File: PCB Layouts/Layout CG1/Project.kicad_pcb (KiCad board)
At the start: 2 copper layers, 15 x 17.5 mm, 11 parts, among them J1 Conn_01x04

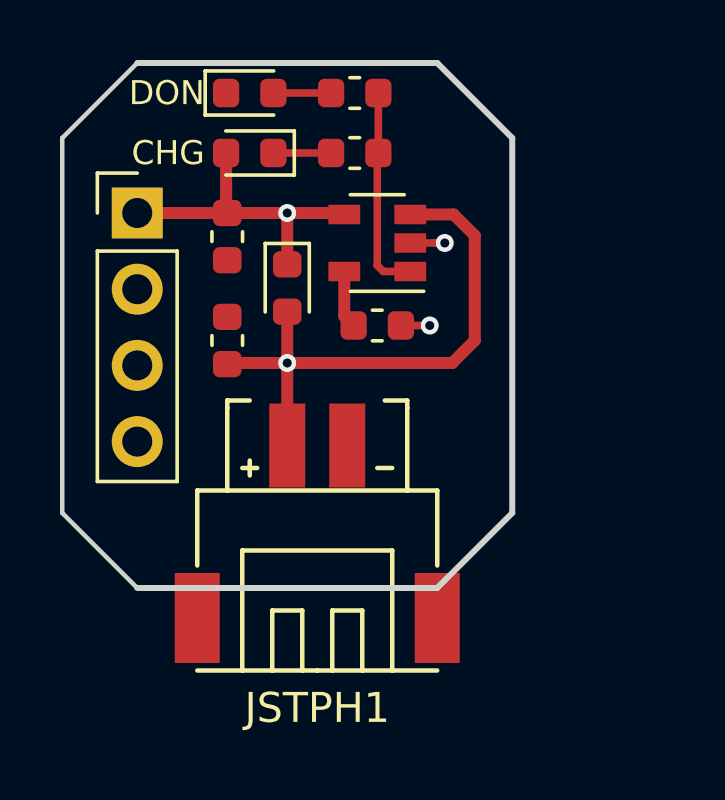
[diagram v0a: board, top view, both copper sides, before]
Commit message: Updated LiPo battery connector footprint and finalized component placement
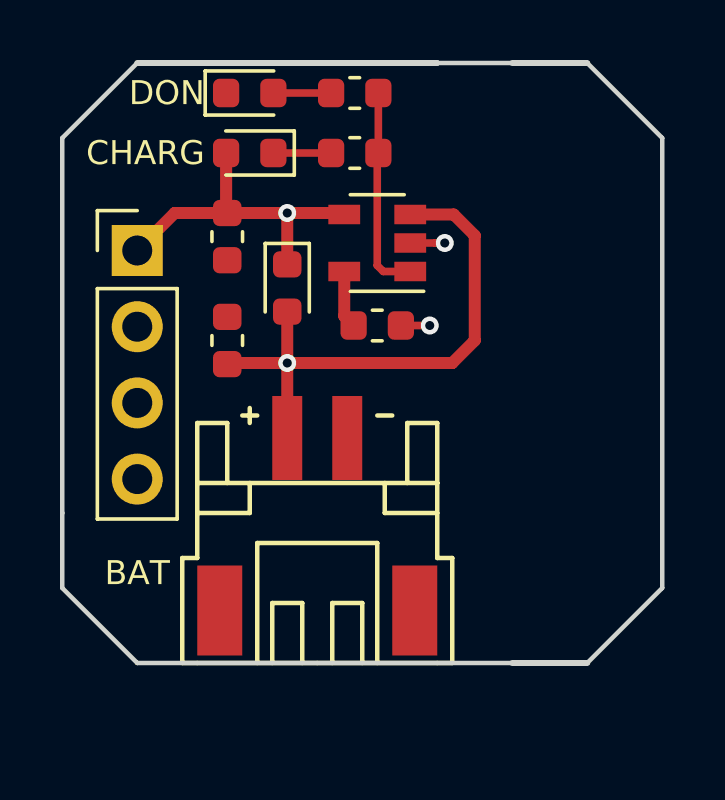
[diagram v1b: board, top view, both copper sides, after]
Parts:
- moved J1 1.25 mm to (100.0, 101.2)
- moved JSTPH1 0.25 mm to (106.0, 112.0)
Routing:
- net VDD: track 10.7 -> 11.2 mm
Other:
- board size 15 x 17.5 mm -> 20 x 20 mm
- board text added: "BAT"
- board text added: "CHARG"
- board text removed: "CHG"

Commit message: Fixed the mounting holes with a simple custom footprint and generated the Gerber files for Layout CG1
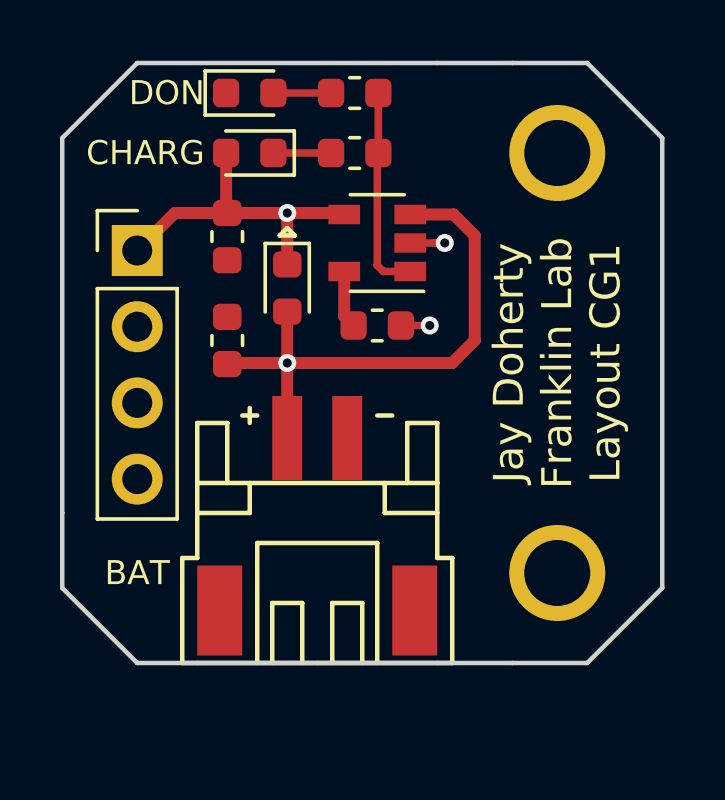
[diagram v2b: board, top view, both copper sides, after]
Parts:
- added MH1: MountingHole, Custom_Footprint_Library:MountingHole_2.2mm, F.Cu at (114.0, 98.0)
- added MH2: MountingHole, Custom_Footprint_Library:MountingHole_2.2mm, F.Cu at (114.0, 112.0)
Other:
- board text added: "Jay Doherty Franklin Lab Layout CG1"
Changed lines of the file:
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@@
   (general
     (thickness 1.6)
-    (drawings 17)
+    (drawings 21)
     (tracks 41)
     (zones 0)
-    (modules 11)
+    (modules 13)
     (nets 10)
   )
@@
   )
   (setup
-    (last_trace_width 0.4)
+    (last_trace_width 0.254)
     (user_trace_width 0.4)
     (trace_clearance 0.254)
@@
     (zone_45_only no)
     (trace_min 0.2)
-    (segment_width 0.2)
+    (segment_width 0.15)
     (edge_width 0.15)
     (via_size 0.6)
@@
     (mod_text_size 1 1)
     (mod_text_width 0.15)
-    (pad_size 1.524 1.524)
-    (pad_drill 0.762)
+    (pad_size 2.2 2.2)
+    (pad_drill 2.2)
     (pad_to_mask_clearance 0.2)
     (aux_axis_origin 0 0)
     (visible_elements FFFFFF7F)
     (pcbplotparams
-      (layerselection 0x010fc_ffffffff)
+      (layerselection 0x010f0_ffffffff)
       (usegerberextensions false)
       (usegerberattributes false)
@@
       (outputformat 1)
       (mirror false)
-      (drillshape 1)
+      (drillshape 0)
       (scaleselection 1)
-      (outputdirectory ""))
+      (outputdirectory "Gerbers/"))
   )
   (net 0 "")
@@
       (effects (font (size 1 1) (thickness 0.15)))
     )
-    (fp_text value 5k (at 2.5 0) (layer F.Fab)
+    (fp_text value 5k (at 0 0) (layer F.Fab)
       (effects (font (size 1 1) (thickness 0.15)))
     )
@@
     )
   )
+  (module Custom_Footprint_Library:MountingHole_2.2mm (layer F.Cu)
+    (at 114 98)
+    (fp_text reference MH1 (at 0 -2.5) (layer F.SilkS) hide
+      (effects (font (size 1 1) (thickness 0.15)))
+    )
+    (fp_text value MountingHole (at 0 2.5) (layer F.Fab) hide
+      (effects (font (size 1 1) (thickness 0.15)))
+    )
+    (pad "" thru_hole circle (at 0 0) (size 3.2 3.2) (drill 2.2) (layers *.Cu *.Mask))
+  )
+  (module Custom_Footprint_Library:MountingHole_2.2mm (layer F.Cu)
+    (at 114 112)
+    (fp_text reference MH2 (at 0 -2.5) (layer F.SilkS) hide
+      (effects (font (size 1 1) (thickness 0.15)))
+    )
+    (fp_text value MountingHole (at 0 2.5) (layer F.Fab) hide
+      (effects (font (size 1 1) (thickness 0.15)))
+    )
+    (pad "" thru_hole circle (at 0 0) (size 3.2 3.2) (drill 2.2) (layers *.Cu *.Mask))
+  )
+  (gr_line (start 105 100.5) (end 104.75 100.75) (layer F.SilkS) (width 0.15))
+  (gr_line (start 105.25 100.75) (end 105 100.5) (layer F.SilkS) (width 0.15))
+  (gr_line (start 104.75 100.75) (end 105.25 100.75) (layer F.SilkS) (width 0.15))
+  (gr_text "Jay Doherty\nFranklin Lab\nLayout CG1" (at 114 105 90) (layer F.SilkS)
+    (effects (font (size 1 1) (thickness 0.15)))
+  )
   (gr_text BAT (at 100 112) (layer F.SilkS)
     (effects (font (size 0.8 0.8) (thickness 0.15)))
   )
-  (gr_line (start 112.5 95) (end 115 95) (layer Edge.Cuts) (width 0.2))
-  (gr_line (start 112.5 115) (end 115 115) (layer Edge.Cuts) (width 0.2))
+  (gr_line (start 112.5 95) (end 115 95) (layer Edge.Cuts) (width 0.15))
+  (gr_line (start 112.5 115) (end 115 115) (layer Edge.Cuts) (width 0.15))
   (gr_line (start 97.5 112.5) (end 97.5 110) (layer Edge.Cuts) (width 0.15))
   (gr_line (start 100 115) (end 97.5 112.5) (layer Edge.Cuts) (width 0.15))
@@
   (gr_line (start 115 95) (end 117.5 97.5) (layer Edge.Cuts) (width 0.15))
   (gr_line (start 110 95) (end 112.5 95) (layer Edge.Cuts) (width 0.15))
-  (gr_line (start 100 95) (end 110 95) (layer Edge.Cuts) (width 0.2))
+  (gr_line (start 100 95) (end 110 95) (layer Edge.Cuts) (width 0.15))
   (gr_line (start 97.5 97.5) (end 97.5 110) (layer Edge.Cuts) (width 0.15))
   (gr_line (start 100 95) (end 97.5 97.5) (layer Edge.Cuts) (width 0.15))

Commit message: Added new PCB layout for a combination BT and battery-powered board. Did initial placement of the 3.3V regulator, LEDs, and CMD jumper. Also fixed the RX/TX pinout for all of these accessory boards
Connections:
- J1 pad 3: RX -> TX
- J1 pad 4: TX -> RX
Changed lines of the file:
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@@
       (net 1 GND))
     (pad 3 thru_hole oval (at 0 5.08) (size 1.7 1.7) (drill 1) (layers *.Cu *.Mask)
+      (net 5 TX))
+    (pad 4 thru_hole oval (at 0 7.62) (size 1.7 1.7) (drill 1) (layers *.Cu *.Mask)
       (net 4 RX))
-    (pad 4 thru_hole oval (at 0 7.62) (size 1.7 1.7) (drill 1) (layers *.Cu *.Mask)
-      (net 5 TX))
     (model ${KISYS3DMOD}/Connector_PinHeader_2.54mm.3dshapes/PinHeader_1x04_P2.54mm_Vertical.wrl
       (at (xyz 0 0 0))
